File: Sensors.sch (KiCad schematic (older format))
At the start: 27 parts, among them P4 CONN_01X04, Q1 PMosfetGen, Q2 PMosfetGen, Q4 PMosfetGen, U1 PIR, U2 MCP6004

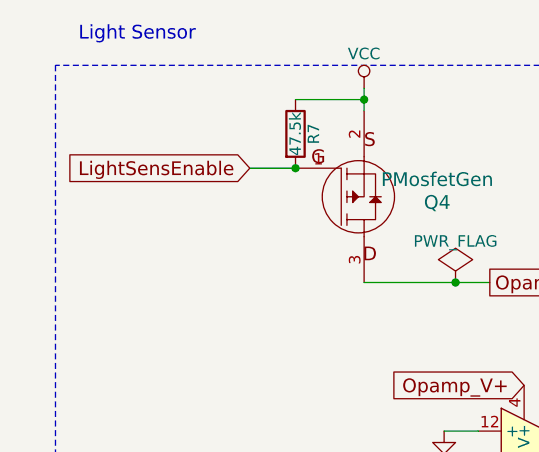
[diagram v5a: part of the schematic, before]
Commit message: Finish work on V2
 * Rework layout
 * Reassign mcu pins
 * Add a capacitor for the RF module

Signed-off-by: Philip Luyckx <philip.luyckx@gmail.com>
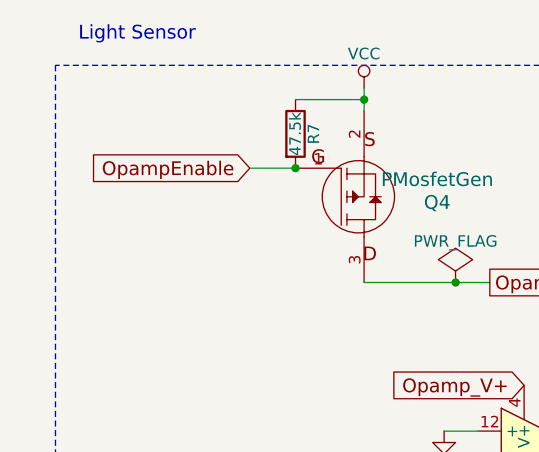
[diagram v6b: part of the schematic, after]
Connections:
- net LightSensEnable renamed OpampEnable
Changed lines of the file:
@@
 $EndDescr
 $Comp
-L +5V #PWR018
+L +5V #PWR017
 U 1 1 56622EB6
 P 6150 1000
-F 0 "#PWR018" H 6150 850 50  0001 C CNN
+F 0 "#PWR017" H 6150 850 50  0001 C CNN
 F 1 "+5V" H 6150 1140 50  0000 C CNN
 F 2 "" H 6150 1000 60  0000 C CNN
@@
 $EndComp
 $Comp
-L GND #PWR019
+L GND #PWR018
 U 1 1 56622ECA
 P 5300 3050
-F 0 "#PWR019" H 5300 2800 50  0001 C CNN
+F 0 "#PWR018" H 5300 2800 50  0001 C CNN
 F 1 "GND" H 5300 2900 50  0000 C CNN
 F 2 "" H 5300 3050 60  0000 C CNN
@@
 $EndComp
 Text GLabel 1500 1250 0    60   Input ~ 0
-LightSensEnable
+OpampEnable
 Text GLabel 3150 2500 2    60   Output ~ 0
 ADC_Light
@@
 $EndComp
 $Comp
-L +5V #PWR020
+L +5V #PWR019
 U 1 1 566301AC
 P 1900 4350
-F 0 "#PWR020" H 1900 4200 50  0001 C CNN
+F 0 "#PWR019" H 1900 4200 50  0001 C CNN
 F 1 "+5V" H 1900 4490 50  0000 C CNN
 F 2 "" H 1900 4350 60  0000 C CNN
@@
 DHT22_Enable
 $Comp
-L GND #PWR021
+L GND #PWR020
 U 1 1 566301BD
 P 1900 5650
-F 0 "#PWR021" H 1900 5400 50  0001 C CNN
+F 0 "#PWR020" H 1900 5400 50  0001 C CNN
 F 1 "GND" H 1900 5500 50  0000 C CNN
 F 2 "" H 1900 5650 60  0000 C CNN
@@
 $EndComp
 $Comp
-L GND #PWR022
+L GND #PWR021
 U 1 1 56637ADC
 P 6150 2150
-F 0 "#PWR022" H 6150 1900 50  0001 C CNN
+F 0 "#PWR021" H 6150 1900 50  0001 C CNN
 F 1 "GND" H 6150 2000 50  0000 C CNN
 F 2 "" H 6150 2150 60  0000 C CNN
@@
 	6450 1950 6550 1950
 $Comp
-L GND #PWR023
+L GND #PWR022
 U 1 1 5662F07B
 P 2000 3050
-F 0 "#PWR023" H 2000 2800 50  0001 C CNN
+F 0 "#PWR022" H 2000 2800 50  0001 C CNN
 F 1 "GND" H 2000 2900 50  0000 C CNN
 F 2 "" H 2000 3050 60  0000 C CNN
@@
 $EndComp
 $Comp
-L VCC #PWR024
+L VCC #PWR023
 U 1 1 56A50243
 P 6750 2600
-F 0 "#PWR024" H 6750 2450 50  0001 C CNN
+F 0 "#PWR023" H 6750 2450 50  0001 C CNN
 F 1 "VCC" H 6750 2750 50  0000 C CNN
 F 2 "" H 6750 2600 50  0000 C CNN
@@
 $EndComp
 $Comp
-L GND #PWR025
+L GND #PWR024
 U 1 1 56A50277
 P 6750 3100
-F 0 "#PWR025" H 6750 2850 50  0001 C CNN
+F 0 "#PWR024" H 6750 2850 50  0001 C CNN
 F 1 "GND" H 6750 2950 50  0000 C CNN
 F 2 "" H 6750 3100 50  0000 C CNN
@@
 Connection ~ 6750 2650
 $Comp
-L GND #PWR026
+L GND #PWR025
 U 1 1 56A503A9
 P 6200 4450
-F 0 "#PWR026" H 6200 4200 50  0001 C CNN
+F 0 "#PWR025" H 6200 4200 50  0001 C CNN
 F 1 "GND" H 6200 4300 50  0000 C CNN
 F 2 "" H 6200 4450 50  0000 C CNN
@@
 $EndComp
 $Comp
-L GND #PWR027
+L GND #PWR026
 U 1 1 56A504D9
 P 7250 3450
-F 0 "#PWR027" H 7250 3200 50  0001 C CNN
+F 0 "#PWR026" H 7250 3200 50  0001 C CNN
 F 1 "GND" H 7250 3300 50  0000 C CNN
 F 2 "" H 7250 3450 50  0000 C CNN
@@
 $EndComp
 $Comp
-L GND #PWR028
+L GND #PWR027
 U 1 1 56A51066
 P 7800 4350
-F 0 "#PWR028" H 7800 4100 50  0001 C CNN
+F 0 "#PWR027" H 7800 4100 50  0001 C CNN
 F 1 "GND" H 7800 4200 50  0000 C CNN
 F 2 "" H 7800 4350 50  0000 C CNN
@@
 Connection ~ 6800 4150
 $Comp
-L GND #PWR029
+L GND #PWR028
 U 1 1 56A51417
 P 6800 4700
-F 0 "#PWR029" H 6800 4450 50  0001 C CNN
+F 0 "#PWR028" H 6800 4450 50  0001 C CNN
 F 1 "GND" H 6800 4550 50  0000 C CNN
 F 2 "" H 6800 4700 50  0000 C CNN
@@
 	8500 4300 8500 4050
 $Comp
-L GND #PWR030
+L GND #PWR029
 U 1 1 56A515AA
 P 8500 4600
-F 0 "#PWR030" H 8500 4350 50  0001 C CNN
+F 0 "#PWR029" H 8500 4350 50  0001 C CNN
 F 1 "GND" H 8500 4450 50  0000 C CNN
 F 2 "" H 8500 4600 50  0000 C CNN
@@
 	11150 750  7850 750
 $Comp
-L GND #PWR031
+L GND #PWR030
 U 1 1 56A51FEC
 P 2700 2800
-F 0 "#PWR031" H 2700 2550 50  0001 C CNN
+F 0 "#PWR030" H 2700 2550 50  0001 C CNN
 F 1 "GND" H 2700 2650 50  0000 C CNN
 F 2 "" H 2700 2800 50  0000 C CNN
@@
 Opamp_V+
 $Comp
-L VCC #PWR032
+L VCC #PWR031
 U 1 1 56B3C197
 P 2000 900
-F 0 "#PWR032" H 2000 750 50  0001 C CNN
+F 0 "#PWR031" H 2000 750 50  0001 C CNN
 F 1 "VCC" H 2000 1050 50  0000 C CNN
 F 2 "" H 2000 900 50  0000 C CNN
@@
 	2000 2600 2000 2650
 $Comp
-L GND #PWR033
+L GND #PWR032
 U 1 1 56B3CEE7
 P 2350 2400
-F 0 "#PWR033" H 2350 2150 50  0001 C CNN
+F 0 "#PWR032" H 2350 2150 50  0001 C CNN
 F 1 "GND" H 2350 2250 50  0000 C CNN
 F 2 "" H 2350 2400 50  0000 C CNN
@@
 	2000 1750 2550 1750
 $Comp
-L PWR_FLAG #FLG034
+L PWR_FLAG #FLG033
 U 1 1 56B4EE8F
 P 2400 1750
-F 0 "#FLG034" H 2400 1845 50  0001 C CNN
+F 0 "#FLG033" H 2400 1845 50  0001 C CNN
 F 1 "PWR_FLAG" H 2400 1930 50  0000 C CNN
 F 2 "" H 2400 1750 50  0000 C CNN
